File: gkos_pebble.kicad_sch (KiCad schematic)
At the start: 1 part, among them J1 10129383-906002BLF

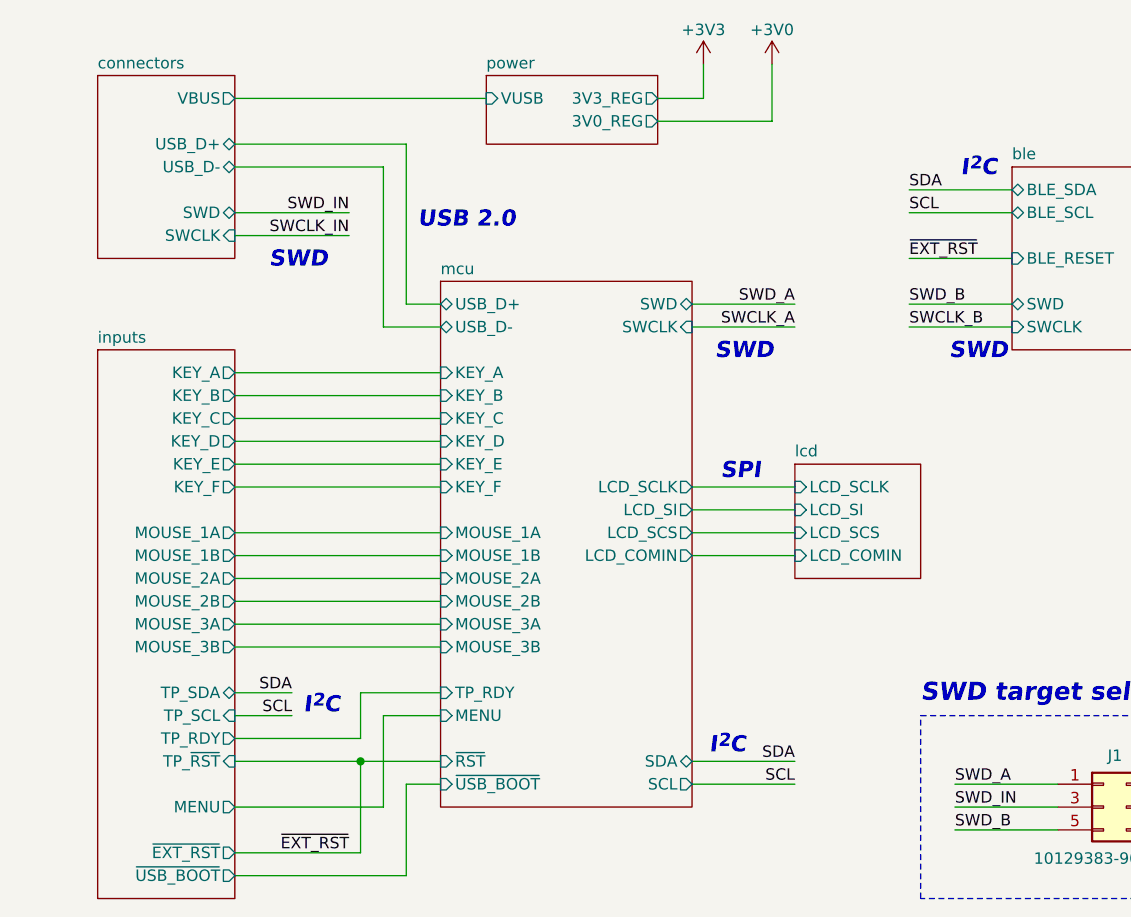
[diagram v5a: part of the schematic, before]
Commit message: added testpoints
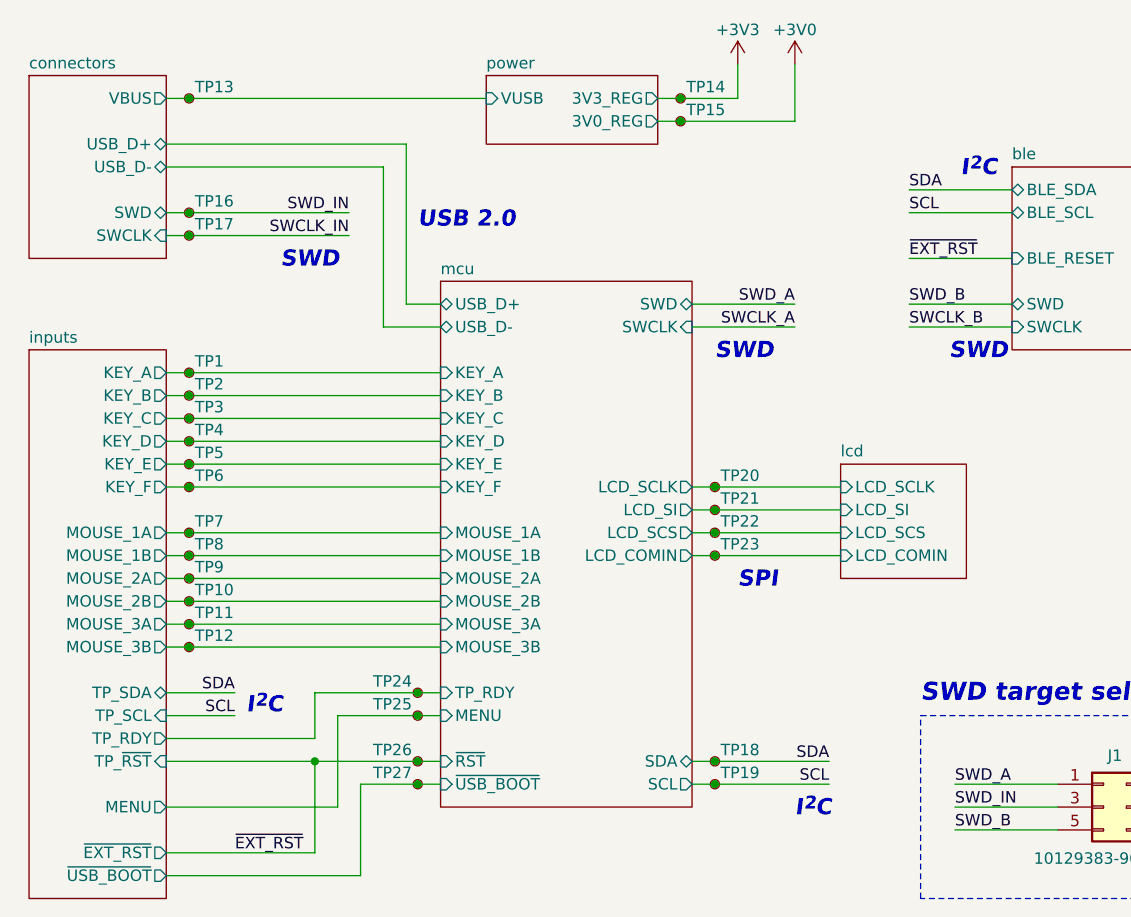
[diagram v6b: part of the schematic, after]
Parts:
- added TP1, TP10, TP11, TP12, TP13, TP14, TP15, TP16, TP17, TP18, TP19, TP2, TP20, TP21, TP22, TP23, TP24, TP25, TP26, TP27, TP3, TP4, TP5, TP6, TP7, TP8, TP9: TestPoint_Small, TestPoint:TestPoint_Pad_D2.0mm, symbol Connector:TestPoint_Small
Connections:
- net +3V0: now also TP15.1
- net +3V3: now also TP14.1
- net SCL: now also TP19.1
- net SDA: now also TP18.1
- net SWCLK_IN: now also TP17.1
- net SWD_IN: now also TP16.1
- net connectors/VBUS: now also TP13.1
- net inputs/KEY_A: now also TP1.1
- net inputs/KEY_B: now also TP2.1
- net inputs/KEY_C: now also TP3.1
- net inputs/KEY_D: now also TP4.1
- net inputs/KEY_E: now also TP5.1
- net inputs/KEY_F: now also TP6.1
- net inputs/MENU: now also TP25.1
- net inputs/MOUSE_1A: now also TP7.1
- net inputs/MOUSE_1B: now also TP8.1
- net inputs/MOUSE_2A: now also TP9.1
- net inputs/MOUSE_2B: now also TP10.1
- net inputs/MOUSE_3A: now also TP11.1
- net inputs/MOUSE_3B: now also TP12.1
- net inputs/TP_RDY: now also TP24.1
- net inputs/~{USB_BOOT}: now also TP27.1
- net lcd/LCD_COMIN: now also TP23.1
- net lcd/LCD_SCLK: now also TP20.1
- net lcd/LCD_SCS: now also TP22.1
- net lcd/LCD_SI: now also TP21.1
- net ~{EXT_RST}: now also TP26.1

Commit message: test points
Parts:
- removed TP1: TestPoint_Small, TestPoint:TestPoint_Pad_D2.0mm, symbol Connector:TestPoint_Small
- added TP13: M2B, TestPoint:TestPoint_Pad_D2.0mm, symbol Connector:TestPoint_Small
- TP1: renamed from TP13; value TestPoint_Small -> VBUS
- TP10: value TestPoint_Small -> M1A
- TP11: value TestPoint_Small -> M1B
- TP12: value TestPoint_Small -> M2A
- TP14: value TestPoint_Small -> M3A
- TP15: value TestPoint_Small -> M3B
- TP16: value TestPoint_Small -> TPRD
- TP17: value TestPoint_Small -> MENU
- TP18: value TestPoint_Small -> RESET
- TP19: value TestPoint_Small -> UBOO
- TP2: value TestPoint_Small -> SWD
- TP20: value TestPoint_Small -> 3V3
- TP21: value TestPoint_Small -> 3V0
- TP22: value TestPoint_Small -> DCL
- TP23: value TestPoint_Small -> DSI
- TP24: value TestPoint_Small -> DCS
- TP25: value TestPoint_Small -> DCI
- TP26: value TestPoint_Small -> SDA
- TP27: value TestPoint_Small -> SCL
- TP3: value TestPoint_Small -> SWCL
- TP4: value TestPoint_Small -> KA
- TP5: value TestPoint_Small -> KB
- TP6: value TestPoint_Small -> KC
- TP7: value TestPoint_Small -> KD
- TP8: value TestPoint_Small -> KE
- TP9: value TestPoint_Small -> KF
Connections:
- net +3V0: now also TP21.1; no longer TP15.1
- net +3V3: now also TP20.1; no longer TP14.1
- net SCL: now also TP27.1; no longer TP19.1
- net SDA: now also TP26.1; no longer TP18.1
- net SWCLK_IN: now also TP3.1; no longer TP17.1
- net SWD_IN: now also TP2.1; no longer TP16.1
- net inputs/KEY_A: now also TP4.1
- net inputs/KEY_B: now also TP5.1; no longer TP2.1
- net inputs/KEY_C: now also TP6.1; no longer TP3.1
- net inputs/KEY_D: now also TP7.1; no longer TP4.1
- net inputs/KEY_E: now also TP8.1; no longer TP5.1
- net inputs/KEY_F: now also TP9.1; no longer TP6.1
- net inputs/MENU: now also TP17.1; no longer TP25.1
- net inputs/MOUSE_1A: now also TP10.1; no longer TP7.1
- net inputs/MOUSE_1B: now also TP11.1; no longer TP8.1
- net inputs/MOUSE_2A: now also TP12.1; no longer TP9.1
- net inputs/MOUSE_2B: now also TP13.1; no longer TP10.1
- net inputs/MOUSE_3A: now also TP14.1; no longer TP11.1
- net inputs/MOUSE_3B: now also TP15.1; no longer TP12.1
- net inputs/TP_RDY: now also TP16.1; no longer TP24.1
- net inputs/~{USB_BOOT}: now also TP19.1; no longer TP27.1
- net lcd/LCD_COMIN: now also TP25.1; no longer TP23.1
- net lcd/LCD_SCLK: now also TP22.1; no longer TP20.1
- net lcd/LCD_SCS: now also TP24.1; no longer TP22.1
- net lcd/LCD_SI: now also TP23.1; no longer TP21.1
- net ~{EXT_RST}: now also TP18.1; no longer TP26.1

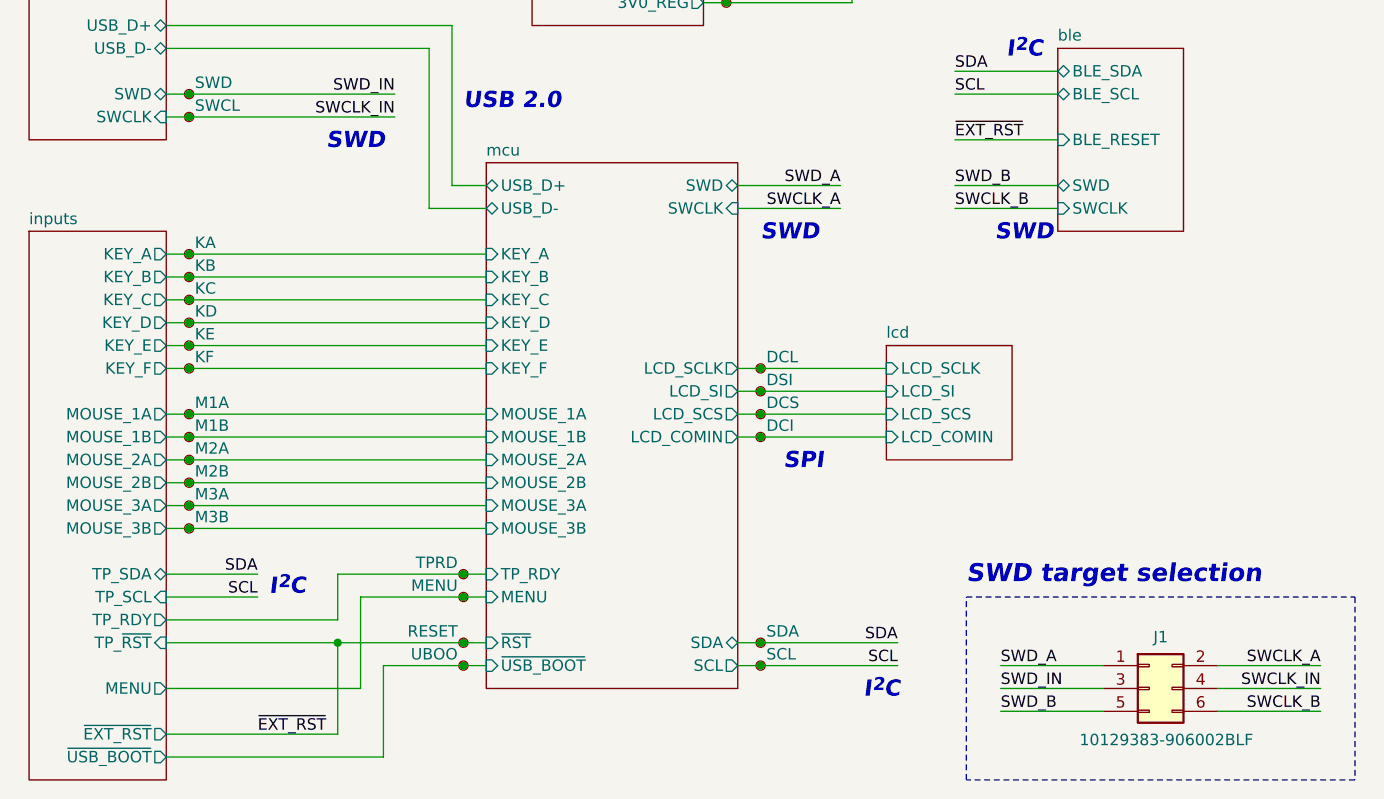
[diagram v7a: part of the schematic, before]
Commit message: finish new mouse button design
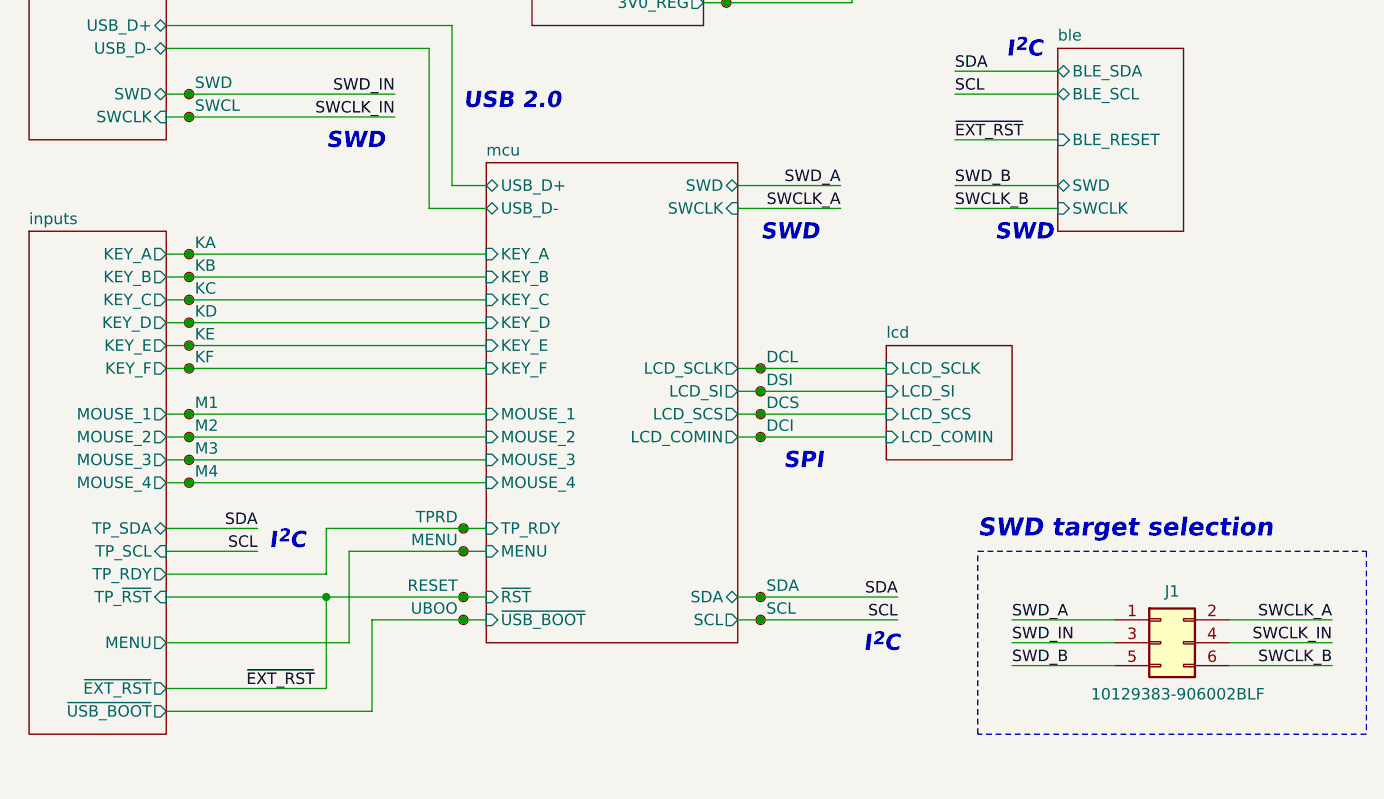
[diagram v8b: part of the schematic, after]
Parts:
- removed TP14: M3A, TestPoint:TestPoint_Pad_D2.0mm, symbol Connector:TestPoint_Small
- removed TP15: M3B, TestPoint:TestPoint_Pad_D2.0mm, symbol Connector:TestPoint_Small
- TP10: value M1A -> M1
- TP11: value M1B -> M2
- TP12: value M2A -> M3
- TP13: value M2B -> M4
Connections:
- net inputs/MOUSE_1A renamed inputs/MOUSE_1
- net inputs/MOUSE_1B renamed inputs/MOUSE_2
- net inputs/MOUSE_2A renamed inputs/MOUSE_3
- net inputs/MOUSE_2B renamed inputs/MOUSE_4
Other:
- sheet inputs ports: added MOUSE_1, MOUSE_2, MOUSE_3, MOUSE_4; removed MOUSE_1A, MOUSE_1B, MOUSE_2A, MOUSE_2B, MOUSE_3A, MOUSE_3B
- sheet mcu ports: added MOUSE_1, MOUSE_2, MOUSE_3, MOUSE_4; removed MOUSE_1A, MOUSE_1B, MOUSE_2A, MOUSE_2B, MOUSE_3A, MOUSE_3B
- moved on the sheet: J1
